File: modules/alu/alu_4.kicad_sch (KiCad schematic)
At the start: 60 parts, among them Q229 2N3906, Q230 2N3906, Q231 2N3906, Q232 2N3906, Q233 2N3906, Q234 2N3906, Q235 2N3906, Q236 2N3906, Q237 2N3904, Q238 2N3904, Q239 2N3904, Q240 2N3904, Q241 2N3904, Q242 2N3904, Q243 2N3904, Q244 2N3904, Q245 2N3904, Q246 2N3904, Q247 2N3904, Q248 2N3904, Q249 2N3904, Q250 2N3904, Q251 2N3904, Q252 2N3904, Q253 2N3906, Q254 2N3906, Q255 2N3906, Q256 2N3906

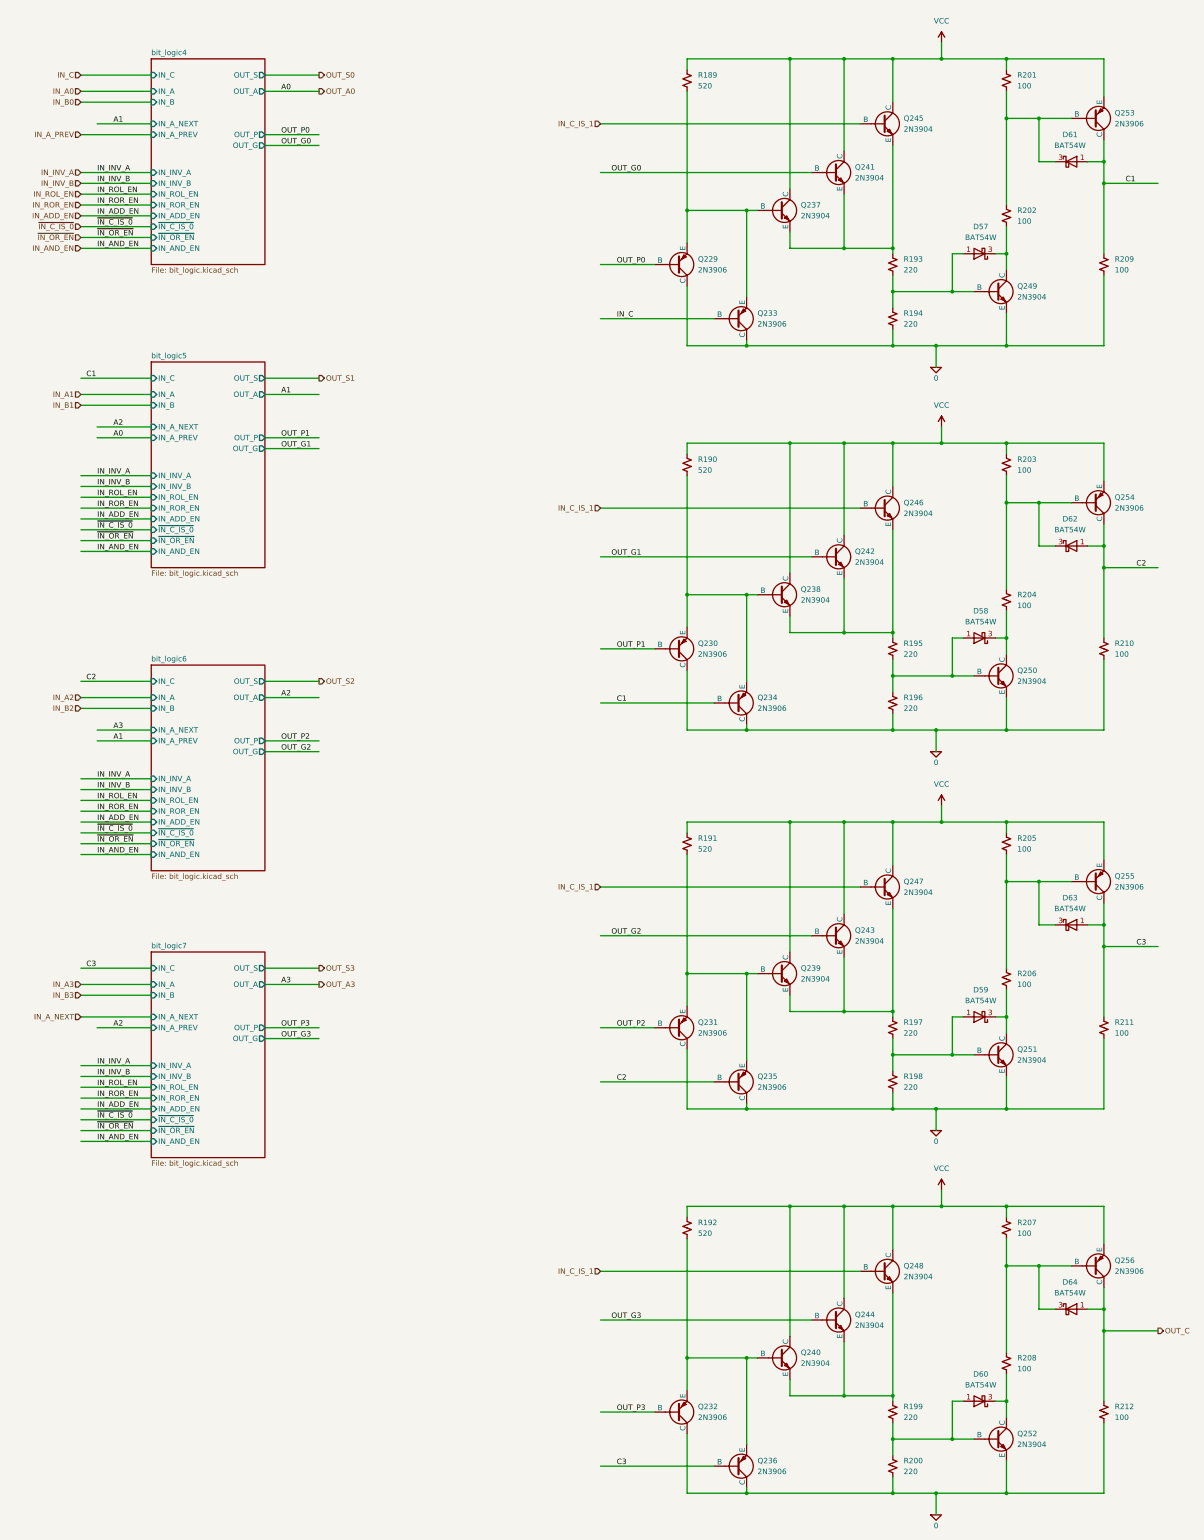
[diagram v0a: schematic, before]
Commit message: Fixed ROL/ROR routing and added flags
This is not fully tested yet, but at least
complete in terms of functionality.

Latency still seems to be less than 350ns.
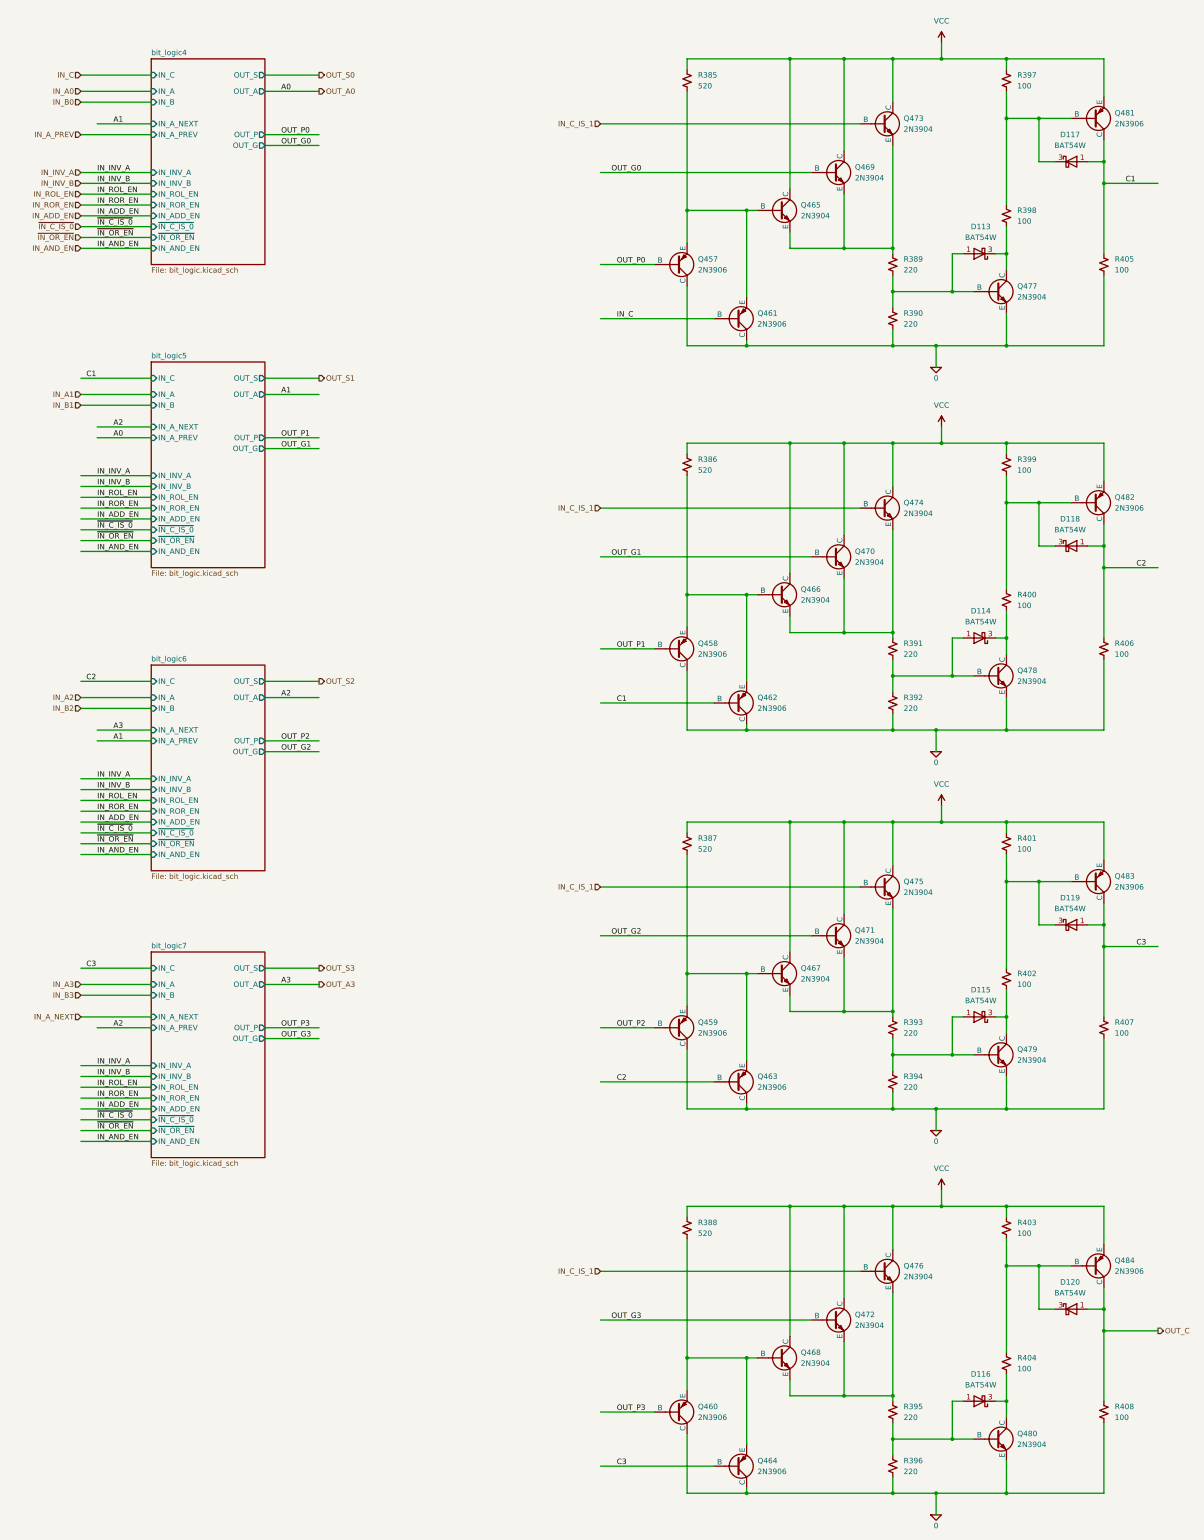
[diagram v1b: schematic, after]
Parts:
- renumbered D57 to D113, D58 to D114, D59 to D115, D60 to D116, D61 to D117, D62 to D118, D63 to D119, D64 to D120, Q229 to Q457, Q230 to Q458, Q231 to Q459, Q232 to Q460, Q233 to Q461, Q234 to Q462, Q235 to Q463, Q236 to Q464, Q237 to Q465, Q238 to Q466, Q239 to Q467, Q240 to Q468, Q241 to Q469, Q242 to Q470, Q243 to Q471, Q244 to Q472, Q245 to Q473, Q246 to Q474, Q247 to Q475, Q248 to Q476, Q249 to Q477, Q250 to Q478, Q251 to Q479, Q252 to Q480, Q253 to Q481, Q254 to Q482, Q255 to Q483, Q256 to Q484, R189 to R385, R190 to R386, R191 to R387, R192 to R388, R193 to R389, R194 to R390, R195 to R391, R196 to R392, R197 to R393, R198 to R394, R199 to R395, R200 to R396, R201 to R397, R202 to R398, R203 to R399, R204 to R400, R205 to R401, R206 to R402, R207 to R403, R208 to R404, R209 to R405, R210 to R406, R211 to R407, R212 to R408
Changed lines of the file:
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@@
 		(dnp no)
 		(fields_autoplaced yes)
-		(property "Reference" "R198"
+		(property "Reference" "R394"
 			(at 227.33 264.1599 0)
 			(effects
@@
 		(on_board yes)
 		(dnp no)
-		(property "Reference" "#GND41"
+		(property "Reference" "#GND35"
 			(at 234.95 102.87 0)
 			(effects
@@
 		(dnp no)
 		(fields_autoplaced yes)
-		(property "Reference" "D60"
+		(property "Reference" "D116"
 			(at 245.4275 334.01 0)
 			(effects
@@
 		(on_board yes)
 		(dnp no)
-		(property "Reference" "Q238"
+		(property "Reference" "Q466"
 			(at 203.2 149.8599 0)
 			(effects
@@
 		(dnp no)
 		(fields_autoplaced yes)
-		(property "Reference" "R208"
+		(property "Reference" "R404"
 			(at 254 330.1999 0)
 			(effects
@@
 		(dnp no)
 		(fields_autoplaced yes)
-		(property "Reference" "Q250"
+		(property "Reference" "Q478"
 			(at 254 168.9099 0)
 			(effects
@@
 		(on_board yes)
 		(dnp no)
-		(property "Reference" "#GND42"
+		(property "Reference" "#GND36"
 			(at 234.95 193.04 0)
 			(effects
@@
 		(dnp no)
 		(fields_autoplaced yes)
-		(property "Reference" "Q241"
+		(property "Reference" "Q469"
 			(at 215.9 50.7999 0)
 			(effects
@@
 		(dnp no)
 		(fields_autoplaced yes)
-		(property "Reference" "Q251"
+		(property "Reference" "Q479"
 			(at 254 257.8099 0)
 			(effects
@@
 		(dnp no)
 		(fields_autoplaced yes)
-		(property "Reference" "R211"
+		(property "Reference" "R407"
 			(at 276.86 251.4599 0)
 			(effects
@@
 		(dnp no)
 		(fields_autoplaced yes)
-		(property "Reference" "D64"
+		(property "Reference" "D120"
 			(at 266.3825 312.42 0)
 			(effects
@@
 		(dnp no)
 		(fields_autoplaced yes)
-		(property "Reference" "D58"
+		(property "Reference" "D114"
 			(at 245.4275 154.94 0)
 			(effects
@@
 		(dnp no)
 		(fields_autoplaced yes)
-		(property "Reference" "#PWR38"
+		(property "Reference" "#PWR32"
 			(at 236.22 25.4 0)
 			(effects
@@
 		(on_board yes)
 		(dnp no)
-		(property "Reference" "Q246"
+		(property "Reference" "Q474"
 			(at 227.33 129.5399 0)
 			(effects
@@
 		(on_board yes)
 		(dnp no)
-		(property "Reference" "Q235"
+		(property "Reference" "Q463"
 			(at 193.04 264.1599 0)
 			(effects
@@
 		(dnp no)
 		(fields_autoplaced yes)
-		(property "Reference" "R205"
+		(property "Reference" "R401"
 			(at 254 208.2799 0)
 			(effects
@@
 		(on_board yes)
 		(dnp no)
-		(property "Reference" "Q247"
+		(property "Reference" "Q475"
 			(at 227.33 218.4399 0)
 			(effects
@@
 		(dnp no)
 		(fields_autoplaced yes)
-		(property "Reference" "R201"
+		(property "Reference" "R397"
 			(at 254 29.2099 0)
 			(effects
@@
 		(on_board yes)
 		(dnp no)
-		(property "Reference" "#GND43"
+		(property "Reference" "#GND38"
 			(at 234.95 281.94 0)
 			(effects
@@
 		(dnp no)
 		(fields_autoplaced yes)
-		(property "Reference" "#PWR41"
+		(property "Reference" "#PWR36"
 			(at 236.22 294.64 0)
 			(effects
@@
 		(dnp no)
 		(fields_autoplaced yes)
-		(property "Reference" "D62"
+		(property "Reference" "D118"
 			(at 266.3825 133.35 0)
 			(effects
@@
 		(on_board yes)
 		(dnp no)
-		(property "Reference" "Q230"
+		(property "Reference" "Q458"
 			(at 179.07 162.5599 0)
 			(effects
@@
 		(dnp no)
 		(fields_autoplaced yes)
-		(property "Reference" "D63"
+		(property "Reference" "D119"
 			(at 266.3825 222.25 0)
 			(effects
@@
 		(dnp no)
 		(fields_autoplaced yes)
-		(property "Reference" "R212"
+		(property "Reference" "R408"
 			(at 276.86 341.6299 0)
 			(effects
@@
 		(dnp no)
 		(fields_autoplaced yes)
-		(property "Reference" "R210"
+		(property "Reference" "R406"
 			(at 276.86 162.5599 0)
 			(effects
@@
 		(dnp no)
 		(fields_autoplaced yes)
-		(property "Reference" "D61"
+		(property "Reference" "D117"
 			(at 266.3825 43.18 0)
 			(effects
@@
 		(dnp no)
 		(fields_autoplaced yes)
-		(property "Reference" "Q252"
+		(property "Reference" "Q480"
 			(at 254 347.9799 0)
 			(effects
@@
 		(dnp no)
 		(fields_autoplaced yes)
-		(property "Reference" "R191"
+		(property "Reference" "R387"
 			(at 179.07 208.2799 0)
 			(effects
@@
 		(dnp no)
 		(fields_autoplaced yes)
-		(property "Reference" "D59"
+		(property "Reference" "D115"
 			(at 245.4275 243.84 0)
 			(effects
@@
 		(dnp no)
 		(fields_autoplaced yes)
-		(property "Reference" "R199"
+		(property "Reference" "R395"
 			(at 227.33 341.6299 0)
 			(effects
@@
 		(dnp no)
 		(fields_autoplaced yes)
-		(property "Reference" "R207"
+		(property "Reference" "R403"
 			(at 254 298.4499 0)
 			(effects
@@
 		(on_board yes)
 		(dnp no)
-		(property "Reference" "Q231"
+		(property "Reference" "Q459"
 			(at 179.07 251.4599 0)
 			(effects
@@
 		(on_board yes)
 		(dnp no)
-		(property "Reference" "Q229"
+		(property "Reference" "Q457"
 			(at 179.07 72.3899 0)
 			(effects
@@
 		(on_board yes)
 		(dnp no)
-		(property "Reference" "Q232"
+		(property "Reference" "Q460"
 			(at 179.07 341.6299 0)
 			(effects
@@
 		(dnp no)
 		(fields_autoplaced yes)
-		(property "Reference" "R200"
+		(property "Reference" "R396"
 			(at 227.33 354.3299 0)
 			(effects
@@
 		(on_board yes)
 		(dnp no)
-		(property "Reference" "Q236"
+		(property "Reference" "Q464"
 			(at 193.04 354.3299 0)
 			(effects
@@
 		(on_board yes)
 		(dnp no)
-		(property "Reference" "Q248"
+		(property "Reference" "Q476"
 			(at 227.33 308.6099 0)
 			(effects
@@
 		(dnp no)
 		(fields_autoplaced yes)
-		(property "Reference" "R203"
+		(property "Reference" "R399"
 			(at 254 119.3799 0)
 			(effects
@@
 		(dnp no)
 		(fields_autoplaced yes)
-		(property "Reference" "#PWR40"
+		(property "Reference" "#PWR35"
 			(at 236.22 204.47 0)
 			(effects
@@
 		(on_board yes)
 		(dnp no)
-		(property "Reference" "Q237"
+		(property "Reference" "Q465"
 			(at 203.2 59.6899 0)
 			(effects
@@
 		(on_board yes)
 		(dnp no)
-		(property "Reference" "Q255"
+		(property "Reference" "Q483"
 			(at 276.86 217.1699 0)
 			(effects
@@
 		(dnp no)
 		(fields_autoplaced yes)
-		(property "Reference" "R193"
+		(property "Reference" "R389"
 			(at 227.33 72.3899 0)
 			(effects
@@
 		(dnp no)
 		(fields_autoplaced yes)
-		(property "Reference" "R202"
+		(property "Reference" "R398"
 			(at 254 60.9599 0)
 			(effects
@@
 		(dnp no)
 		(fields_autoplaced yes)
-		(property "Reference" "Q244"
+		(property "Reference" "Q472"
 			(at 215.9 320.0399 0)
 			(effects
@@
 		(dnp no)
 		(fields_autoplaced yes)
-		(property "Reference" "R197"
+		(property "Reference" "R393"
 			(at 227.33 251.4599 0)
 			(effects
@@
 		(dnp no)
 		(fields_autoplaced yes)
-		(property "Reference" "Q243"
+		(property "Reference" "Q471"
 			(at 215.9 229.8699 0)
 			(effects
@@
 		(on_board yes)
 		(dnp no)
-		(property "Reference" "Q233"
+		(property "Reference" "Q461"
 			(at 193.04 85.0899 0)
 			(effects
@@
 		(dnp no)
 		(fields_autoplaced yes)
-		(property "Reference" "R209"
+		(property "Reference" "R405"
 			(at 276.86 72.3899 0)
 			(effects
@@
 		(dnp no)
 		(fields_autoplaced yes)
-		(property "Reference" "R206"
+		(property "Reference" "R402"
 			(at 254 240.0299 0)
 			(effects
@@
 		(dnp no)
 		(fields_autoplaced yes)
-		(property "Reference" "Q242"
+		(property "Reference" "Q470"
 			(at 215.9 140.9699 0)
 			(effects
@@
 		(on_board yes)
 		(dnp no)
-		(property "Reference" "Q245"
+		(property "Reference" "Q473"
 			(at 227.33 39.3699 0)
 			(effects
@@
 		(dnp no)
 		(fields_autoplaced yes)
-		(property "Reference" "R190"
+		(property "Reference" "R386"
 			(at 179.07 119.3799 0)
 			(effects
@@
 		(on_board yes)
 		(dnp no)
-		(property "Reference" "Q239"
+		(property "Reference" "Q467"
 			(at 203.2 238.7599 0)
 			(effects
@@
 		(dnp no)
 		(fields_autoplaced yes)
-		(property "Reference" "R189"
+		(property "Reference" "R385"
 			(at 179.07 29.2099 0)
 			(effects
@@
 		(dnp no)
 		(fields_autoplaced yes)
-		(property "Reference" "R196"
+		(property "Reference" "R392"
 			(at 227.33 175.2599 0)
 			(effects
@@
 		(dnp no)
 		(fields_autoplaced yes)
-		(property "Reference" "Q249"
+		(property "Reference" "Q477"
 			(at 254 78.7399 0)
 			(effects
@@
 		(dnp no)
 		(fields_autoplaced yes)
-		(property "Reference" "R194"
+		(property "Reference" "R390"
 			(at 227.33 85.0899 0)
 			(effects
@@
 		(dnp no)
 		(fields_autoplaced yes)
-		(property "Reference" "D57"
+		(property "Reference" "D113"
 			(at 245.4275 64.77 0)
 			(effects
@@
 		(dnp no)
 		(fields_autoplaced yes)
-		(property "Reference" "#PWR39"
+		(property "Reference" "#PWR33"
 			(at 236.22 115.57 0)
 			(effects
@@
 		(dnp no)
 		(fields_autoplaced yes)
-		(property "Reference" "R204"
+		(property "Reference" "R400"
 			(at 254 151.1299 0)
 			(effects
@@
 		(dnp no)
 		(fields_autoplaced yes)
-		(property "Reference" "R192"
+		(property "Reference" "R388"
 			(at 179.07 298.4499 0)
 			(effects
@@
 		(on_board yes)
 		(dnp no)
-		(property "Reference" "Q254"
+		(property "Reference" "Q482"
 			(at 276.86 128.2699 0)
 			(effects
@@
 		(on_board yes)
 		(dnp no)
-		(property "Reference" "Q253"
+		(property "Reference" "Q481"
 			(at 276.86 38.0999 0)
 			(effects
@@
 		(on_board yes)
 		(dnp no)
-		(property "Reference" "Q256"
+		(property "Reference" "Q484"
 			(at 276.86 307.3399 0)
 			(effects
@@
 		(dnp no)
 		(fields_autoplaced yes)
-		(property "Reference" "R195"
+		(property "Reference" "R391"
 			(at 227.33 162.5599 0)
 			(effects
@@
 		(on_board yes)
 		(dnp no)
-		(property "Reference" "Q234"
+		(property "Reference" "Q462"
 			(at 193.04 175.2599 0)
 			(effects
@@
 		(on_board yes)
 		(dnp no)
-		(property "Reference" "#GND44"
+		(property "Reference" "#GND39"
 			(at 234.95 372.11 0)
 			(effects
@@
 		(on_board yes)
 		(dnp no)
-		(property "Reference" "Q240"
+		(property "Reference" "Q468"
 			(at 203.2 328.9299 0)
 			(effects

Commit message: Small ALU fix.
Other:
- note added: "AND-OR gate to implement CARRY"
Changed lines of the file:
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@@
 	)
 	(junction
+		(at 274.32 25.4)
+		(diameter 0)
+		(color 0 0 0 0)
+	)
+	(junction
 		(at 224.79 80.01)
 		(diameter 0)
@@
 	)
 	(junction
-		(at 236.22 25.4)
-		(diameter 0)
-		(color 0 0 0 0)
-	)
-	(junction
 		(at 213.36 294.64)
 		(diameter 0)
@@
 	(wire
 		(pts
-			(xy 224.79 25.4) (xy 236.22 25.4)
+			(xy 224.79 25.4) (xy 251.46 25.4)
 		)
 		(stroke
@@
 	(wire
 		(pts
+			(xy 274.32 25.4) (xy 251.46 25.4)
+		)
+		(stroke
+			(width 0)
+			(type default)
+		)
+	)
+	(wire
+		(pts
 			(xy 274.32 76.2) (xy 274.32 92.71)
 		)
@@
 	(wire
 		(pts
-			(xy 236.22 21.59) (xy 236.22 25.4)
+			(xy 274.32 22.86) (xy 274.32 25.4)
 		)
 		(stroke
@@
 	(wire
 		(pts
-			(xy 236.22 25.4) (xy 251.46 25.4)
-		)
-		(stroke
-			(width 0)
-			(type default)
-		)
-	)
-	(wire
-		(pts
 			(xy 251.46 33.02) (xy 251.46 39.37)
 		)
@@
 	(wire
 		(pts
-			(xy 251.46 25.4) (xy 274.32 25.4)
-		)
-		(stroke
-			(width 0)
-			(type default)
-		)
-	)
-	(wire
-		(pts
 			(xy 190.5 151.13) (xy 190.5 171.45)
 		)
@@
 		)
 	)
+	(rectangle
+		(start 135.89 13.97)
+		(end 294.64 102.87)
+		(stroke
+			(width 0.0508)
+			(type dash_dot_dot)
+			(color 255 0 0 1)
+		)
+		(fill
+			(type none)
+		)
+	)
+	(text "AND-OR gate to implement CARRY"
+		(exclude_from_sim no)
+		(at 137.16 17.78 0)
+		(effects
+			(font
+				(size 3.81 3.81)
+				(color 255 0 0 1)
+			)
+			(justify left)
+		)
+	)
 	(label "OUT_P2"
 		(at 160.02 252.73 0)
@@
 	(symbol
 		(lib_id "power:VCC")
-		(at 236.22 21.59 0)
+		(at 274.32 22.86 0)
 		(unit 1)
 		(exclude_from_sim no)
@@
 		(fields_autoplaced yes)
 		(property "Reference" "#PWR32"
-			(at 236.22 25.4 0)
+			(at 274.32 26.67 0)
 			(effects
 				(font
@@
 		)
 		(property "Value" "VCC"
-			(at 236.22 16.51 0)
+			(at 274.32 17.78 0)
 			(effects
 				(font
@@
 		)
 		(property "Footprint" ""
-			(at 236.22 21.59 0)
+			(at 274.32 22.86 0)
 			(effects
 				(font
@@
 		)
 		(property "Datasheet" ""
-			(at 236.22 21.59 0)
+			(at 274.32 22.86 0)
 			(effects
 				(font
@@
 		)
 		(property "Description" "Power symbol creates a global label with name \"VCC\""
-			(at 236.22 21.59 0)
+			(at 274.32 22.86 0)
 			(effects
 				(font
